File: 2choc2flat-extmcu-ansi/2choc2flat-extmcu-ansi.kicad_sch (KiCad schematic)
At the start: 138 parts, among them J1 Conn_01x09_Male, J2 Conn_01x05_Male, J3 Conn_01x09_Male, K1 KEYSW, K10 KEYSW, K11 KEYSW, K12 KEYSW, K13 KEYSW, K14 KEYSW, K16 KEYSW, K17 KEYSW, K18 KEYSW, K19 KEYSW, K2 KEYSW, K20 KEYSW, K21 KEYSW, K22 KEYSW, K23 KEYSW, K24 KEYSW, K25 KEYSW, K26 KEYSW, K27 KEYSW, K28 KEYSW, K29 KEYSW, K3 KEYSW, K31 KEYSW, K31-1 KEYSW, K32 KEYSW, K33 KEYSW, K34 KEYSW, K35 KEYSW, K36 KEYSW, K37 KEYSW, K38 KEYSW, K39 KEYSW, K4 KEYSW, K40 KEYSW, K41 KEYSW, K42 KEYSW, K44 KEYSW, K46 KEYSW, K47 KEYSW, K48 KEYSW, K49 KEYSW, K5 KEYSW, K50 KEYSW, K51 KEYSW, K52 KEYSW, K53 KEYSW, K54 KEYSW, K55 KEYSW, K56 KEYSW, K57 KEYSW, K58 KEYSW, K59 KEYSW, K6 KEYSW, K61 KEYSW, K62 KEYSW, K63 KEYSW, K67 KEYSW, K7 KEYSW, K71 KEYSW, K72 KEYSW, K73 KEYSW, K74 KEYSW, K75 KEYSW, K8 KEYSW, K9 KEYSW

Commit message: fix stab orientation to plate
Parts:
- K67: footprint Switch_Keyboard_Hotswap_Kailh_mine:SW_Hotswap_Kailh_Choc_V2_6.25u_North_Gateron_LP_Stabs -> Switch_Keyboard_Hotswap_Kailh_mine:SW_Hotswap_Kailh_Choc_V2_6.25u
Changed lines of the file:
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@@
       (effects (font (size 1.524 1.524)) hide)
     )
-    (property "Footprint" "Switch_Keyboard_Hotswap_Kailh_mine:SW_Hotswap_Kailh_Choc_V2_6.25u_North_Gateron_LP_Stabs" (id 2) (at 161.29 222.25 0)
+    (property "Footprint" "Switch_Keyboard_Hotswap_Kailh_mine:SW_Hotswap_Kailh_Choc_V2_6.25u" (id 2) (at 161.29 222.25 0)
       (effects (font (size 1.524 1.524)) hide)
     )
@@
     )
     (path "/00000000-0000-0000-0000-00005c555e38"
-      (reference "K67") (unit 1) (value "KEYSW") (footprint "Switch_Keyboard_Hotswap_Kailh_mine:SW_Hotswap_Kailh_Choc_V2_6.25u_North_Gateron_LP_Stabs")
+      (reference "K67") (unit 1) (value "KEYSW") (footprint "Switch_Keyboard_Hotswap_Kailh_mine:SW_Hotswap_Kailh_Choc_V2_6.25u")
     )
     (path "/00000000-0000-0000-0000-00005cb7e685"

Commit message: wip attempting rerouting
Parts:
- added DI1: LED, LED_SMD:LED_1206_3216Metric_ReverseMount_Hole1.8x2.4mm, symbol Device:LED
- added R1: 330R, Resistor_SMD:R_0603_1608Metric, symbol Device:R_Small_US
- D1, D10, D11, D12, D13, D14, D16, D17, D18, D19, D2, D20, D21, D22, D23, D24, D25, D26, D27, D28, D29, D3, D31, D32, D33, D34, D35, D36, D37, D38, D39, D4, D40, D41, D42, D44, D46, D47, D48, D49, D5, D50, D51, D52, D53, D54, D55, D56, D57, D58, D59, D6, D61, D62, D63, D67, D7, D71, D72, D73, D74, D75, D8, D9: footprint Diode_SMD:D_0805_2012Metric -> Diode_SMD:D_SOD-323_HandSoldering
- K8: footprint Switch_Keyboard_Kailh_mine:SW_Kailh_Choc_V2_1.00u -> Switch_Keyboard_Hotswap_Kailh_mine:SW_Hotswap_Kailh_Choc_V2_1.00u
- S3: footprint MountingHole:MountingHole_2.2mm_M2_Pad_TopOnly -> MountingHole:MountingHole_2.2mm_M2_Pad_Via
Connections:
- net +3V3: now also J3.3 (Pin_3); no longer J1.3 (Pin_3)
- net +5V: now also J3.1 (Pin_1); no longer J1.1 (Pin_1)
- net GND: now also J3.2 (Pin_2), DI1.1 (K); no longer J1.2 (Pin_2)
- net col0: now also J3.9 (Pin_9), K16.1, K46.1, K61.1; no longer J1.4 (Pin_4), K16.2, K46.2, K61.2
- net col1: now also J3.4 (Pin_4), K17.1, K2.1, K32.1, K47.1; no longer J1.5 (Pin_5), K17.2, K2.2, K32.2, K47.2
- net col10: now also J1.5 (Pin_5); no longer J3.5 (Pin_5)
- net col11: now also J1.4 (Pin_4); no longer J3.4 (Pin_4)
- net col12: now also J1.3 (Pin_3); no longer J3.3 (Pin_3)
- net col13: now also J1.2 (Pin_2), K29.1, K44.1; no longer J3.2 (Pin_2), K29.2, K44.2
- net col2: now also J3.5 (Pin_5), K3.1, K48.1, K63.1; no longer J1.6 (Pin_6), K3.2, K48.2, K63.2
- net col3: now also J3.6 (Pin_6); no longer J1.7 (Pin_7)
- net col4: now also J3.7 (Pin_7); no longer J1.8 (Pin_8)
- net col5: now also J3.8 (Pin_8); no longer J1.9 (Pin_9)
- net col6: now also K37.1, K67.1; no longer K37.2, K67.2
- net col8: now also J1.7 (Pin_7); no longer J3.7 (Pin_7)
- net col9: now also J1.6 (Pin_6), K71.1; no longer J3.6 (Pin_6), K71.2
- net row3: now also J1.9 (Pin_9); no longer J3.9 (Pin_9)
- net row4: now also J1.8 (Pin_8); no longer J3.8 (Pin_8)
- net at D2.2 (A): now also K2.2; no longer K2.1
- net at D3.2 (A): now also K3.2; no longer K3.1
- net at D16.2 (A): now also K16.2; no longer K16.1
- net at D17.2 (A): now also K17.2; no longer K17.1
- net at D29.2 (A): now also K29.2; no longer K29.1
- net at D32.2 (A): now also K32.2; no longer K32.1
- net at D37.2 (A): now also K37.2; no longer K37.1
- net at D44.2 (A): now also K44.2; no longer K44.1
- net at D46.2 (A): now also K46.2; no longer K46.1
- net at D48.2 (A): now also K48.2; no longer K48.1
- net at D61.2 (A): now also K61.2; no longer K61.1
- net at D63.2 (A): now also K63.2; no longer K63.1
- net at D67.2 (A): now also K67.2; no longer K67.1
- net at D71.2 (A): now also K71.2; no longer K71.1
- net at D47.2 (A): now also K47.2; no longer K47.1
- new net: DI1.2 (A), R1.2
- new net caps: J1.1 (Pin_1), R1.1
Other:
- moved on the sheet: K44

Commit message: routing complete
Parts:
- S3: footprint MountingHole:MountingHole_2.2mm_M2_Pad_Via -> MountingHole:MountingHole_2.2mm_M2_Pad_TopOnly
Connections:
- net col0: now also J3.4 (Pin_4); no longer J3.9 (Pin_9)
- net col1: now also J3.5 (Pin_5); no longer J3.4 (Pin_4)
- net col10: now also J1.4 (Pin_4); no longer J1.5 (Pin_5)
- net col11: now also J1.5 (Pin_5); no longer J1.4 (Pin_4)
- net col12: now also J1.6 (Pin_6); no longer J1.3 (Pin_3)
- net col13: now also J1.7 (Pin_7); no longer J1.2 (Pin_2)
- net col2: now also J3.6 (Pin_6); no longer J3.5 (Pin_5)
- net col3: now also J3.7 (Pin_7); no longer J3.6 (Pin_6)
- net col4: now also J3.8 (Pin_8); no longer J3.7 (Pin_7)
- net col5: now also J3.9 (Pin_9); no longer J3.8 (Pin_8)
- net col6: now also J2.5 (Pin_5); no longer J2.4 (Pin_4)
- net col7: now also J2.4 (Pin_4); no longer J2.5 (Pin_5)
- net col8: now also J1.2 (Pin_2); no longer J1.7 (Pin_7)
- net col9: now also J1.3 (Pin_3); no longer J1.6 (Pin_6)
- net row0: now also J2.3 (Pin_3); no longer J2.1 (Pin_1)
- net row2: now also J2.1 (Pin_1); no longer J2.3 (Pin_3)

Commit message: rev 1.3 layouts
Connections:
- net col10: now also J1.5 (Pin_5); no longer J1.4 (Pin_4)
- net col11: now also J1.4 (Pin_4); no longer J1.5 (Pin_5)
- net col12: now also J1.3 (Pin_3); no longer J1.6 (Pin_6)
- net col13: now also J1.2 (Pin_2); no longer J1.7 (Pin_7)
- net col8: now also J1.7 (Pin_7); no longer J1.2 (Pin_2)
- net col9: now also J1.6 (Pin_6); no longer J1.3 (Pin_3)

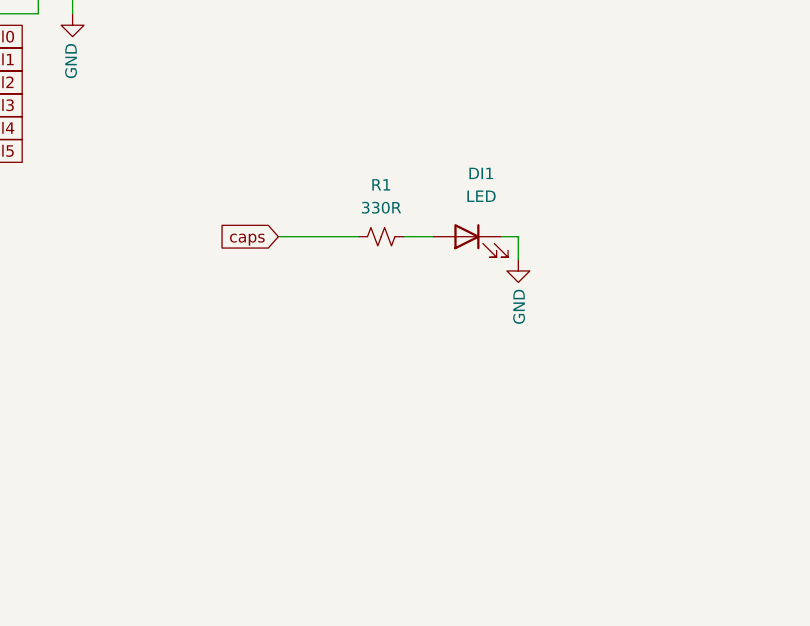
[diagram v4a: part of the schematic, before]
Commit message: add second caps led, minor tweaks
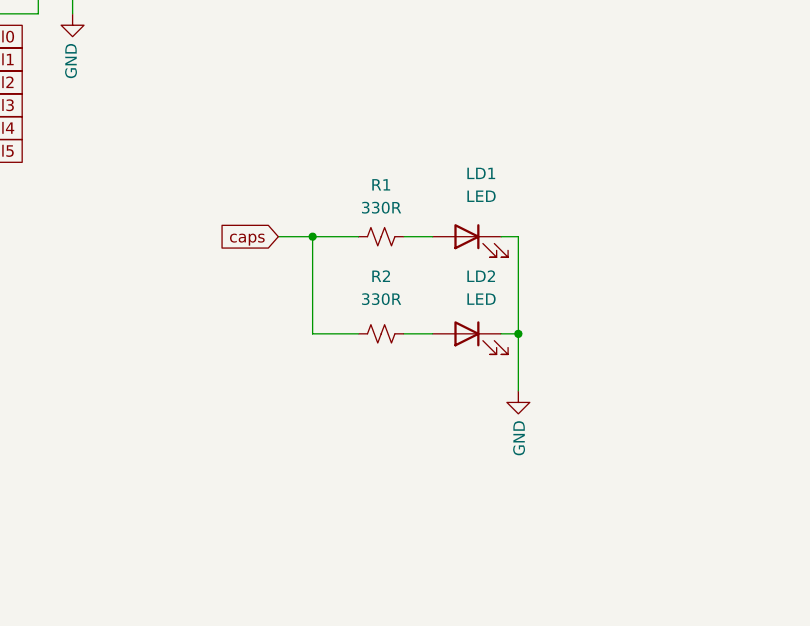
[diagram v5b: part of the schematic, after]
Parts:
- added LD2: LED, LED_SMD:LED_1206_3216Metric_ReverseMount_Hole1.8x2.4mm, symbol Device:LED
- added R2: 330R, Resistor_SMD:R_0603_1608Metric, symbol Device:R_Small_US
- renumbered DI1 to LD1
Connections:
- net GND: now also LD2.1 (K)
- net caps: now also R2.1
- new net: LD2.2 (A), R2.2
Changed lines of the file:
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@@
   (junction (at 311.15 161.29) (diameter 0) (color 0 0 0 0)
   )
+  (junction (at 163.83 87.63) (diameter 0) (color 0 0 0 0)
+  )
   (junction (at 87.63 146.05) (diameter 0) (color 0 0 0 0)
   )
@@
   (junction (at 270.51 146.05) (diameter 0) (color 0 0 0 0)
   )
+  (junction (at 140.97 76.835) (diameter 0) (color 0 0 0 0)
+  )
   (junction (at 250.19 201.93) (diameter 0) (color 0 0 0 0)
   )
@@
     (stroke (width 0) (type default) (color 0 0 0 0))
   )
+  (wire (pts (xy 140.97 87.63) (xy 146.05 87.63))
+    (stroke (width 0) (type default) (color 0 0 0 0))
+  )
   (wire (pts (xy 29.21 222.25) (xy 31.75 222.25))
     (stroke (width 0) (type default) (color 0 0 0 0))
@@
     (stroke (width 0) (type default) (color 0 0 0 0))
   )
+  (wire (pts (xy 163.83 87.63) (xy 163.83 93.98))
+    (stroke (width 0) (type default) (color 0 0 0 0))
+  )
   (wire (pts (xy 252.73 161.29) (xy 255.27 161.29))
     (stroke (width 0) (type default) (color 0 0 0 0))
@@
     (stroke (width 0) (type default) (color 0 0 0 0))
   )
-  (wire (pts (xy 163.83 76.835) (xy 163.83 79.375))
+  (wire (pts (xy 163.83 76.835) (xy 163.83 87.63))
     (stroke (width 0) (type default) (color 0 0 0 0))
   )
@@
     (stroke (width 0) (type default) (color 0 0 0 0))
   )
+  (wire (pts (xy 140.97 76.835) (xy 146.05 76.835))
+    (stroke (width 0) (type default) (color 0 0 0 0))
+  )
   (wire (pts (xy 110.49 52.07) (xy 101.6 52.07))
     (stroke (width 0) (type default) (color 0 0 0 0))
@@
     (stroke (width 0) (type default) (color 0 0 0 0))
   )
+  (wire (pts (xy 151.13 87.63) (xy 154.305 87.63))
+    (stroke (width 0) (type default) (color 0 0 0 0))
+  )
   (wire (pts (xy 171.45 184.15) (xy 171.45 181.61))
     (stroke (width 0) (type default) (color 0 0 0 0))
@@
     (stroke (width 0) (type default) (color 0 0 0 0))
   )
-  (wire (pts (xy 137.16 76.835) (xy 146.05 76.835))
+  (wire (pts (xy 137.16 76.835) (xy 140.97 76.835))
     (stroke (width 0) (type default) (color 0 0 0 0))
   )
@@
     (stroke (width 0) (type default) (color 0 0 0 0))
   )
+  (wire (pts (xy 161.925 87.63) (xy 163.83 87.63))
+    (stroke (width 0) (type default) (color 0 0 0 0))
+  )
   (wire (pts (xy 171.45 204.47) (xy 171.45 201.93))
     (stroke (width 0) (type default) (color 0 0 0 0))
@@
     (stroke (width 0) (type default) (color 0 0 0 0))
   )
+  (wire (pts (xy 140.97 76.835) (xy 140.97 87.63))
+    (stroke (width 0) (type default) (color 0 0 0 0))
+  )
   (global_label "col8" (shape input) (at 209.55 130.81 180)
     (effects (font (size 1.27 1.27)) (justify right))
@@
     (pin "2")
   )
-  (symbol (lib_id "Power:GND") (at 163.83 79.375 0) (unit 1)
+  (symbol (lib_id "Power:GND") (at 163.83 93.98 0) (unit 1)
     (in_bom yes) (on_board yes)
-    (property "Reference" "#PWR0103" (id 0) (at 163.83 85.725 0)
+    (property "Reference" "#PWR0103" (id 0) (at 163.83 100.33 0)
       (effects (font (size 1.27 1.27)) hide)
     )
-    (property "Value" "GND" (id 1) (at 163.957 82.6262 90)
+    (property "Value" "GND" (id 1) (at 163.957 97.2312 90)
       (effects (font (size 1.27 1.27)) (justify right))
     )
-    (property "Footprint" "" (id 2) (at 163.83 79.375 0)
+    (property "Footprint" "" (id 2) (at 163.83 93.98 0)
+      (effects (font (size 1.27 1.27)) hide)
+    )
+    (property "Datasheet" "" (id 3) (at 163.83 93.98 0)
+      (effects (font (size 1.27 1.27)) hide)
+    )
+    (pin "1")
+  )
+  (symbol (lib_id "Device:R_Small_US") (at 148.59 87.63 90) (unit 1)
+    (in_bom yes) (on_board yes) (fields_autoplaced)
+    (property "Reference" "R2" (id 0) (at 148.59 81.28 90))
+    (property "Value" "330R" (id 1) (at 148.59 83.82 90))
+    (property "Footprint" "Resistor_SMD:R_0603_1608Metric" (id 2) (at 148.59 87.63 0)
       (effects (font (size 1.27 1.27)) hide)
     )
-    (property "Datasheet" "" (id 3) (at 163.83 79.375 0)
+    (property "Datasheet" "~" (id 3) (at 148.59 87.63 0)
       (effects (font (size 1.27 1.27)) hide)
     )
     (pin "1")
+    (pin "2")
   )
   (symbol (lib_id "Connector:Conn_01x09_Male") (at 81.28 57.15 0) (mirror y) (unit 1)
@@
     (pin "1")
   )
+  (symbol (lib_id "Device:LED") (at 158.115 87.63 0) (mirror y) (unit 1)
+    (in_bom yes) (on_board yes) (fields_autoplaced)
+    (property "Reference" "LD2" (id 0) (at 159.7025 81.28 0))
+    (property "Value" "LED" (id 1) (at 159.7025 83.82 0))
+    (property "Footprint" "LED_SMD:LED_1206_3216Metric_ReverseMount_Hole1.8x2.4mm" (id 2) (at 158.115 87.63 0)
+      (effects (font (size 1.27 1.27)) hide)
+    )
+    (property "Datasheet" "~" (id 3) (at 158.115 87.63 0)
+      (effects (font (size 1.27 1.27)) hide)
+    )
+    (pin "1")
+    (pin "2")
+  )
   (symbol (lib_id "Connector:Conn_01x09_Male") (at 96.52 57.15 0) (unit 1)
     (in_bom yes) (on_board yes)
@@
   (symbol (lib_id "Device:LED") (at 158.115 76.835 0) (mirror y) (unit 1)
     (in_bom yes) (on_board yes) (fields_autoplaced)
-    (property "Reference" "DI1" (id 0) (at 159.7025 69.85 0))
+    (property "Reference" "LD1" (id 0) (at 159.7025 69.85 0))
     (property "Value" "LED" (id 1) (at 159.7025 72.39 0))
     (property "Footprint" "LED_SMD:LED_1206_3216Metric_ReverseMount_Hole1.8x2.4mm" (id 2) (at 158.115 76.835 0)
@@
       (reference "D75") (unit 1) (value "D") (footprint "Diode_SMD:D_SOD-323_HandSoldering")
     )
-    (path "/d2a931d0-1ec6-4bb9-bddb-4815c7c34ed3"
-      (reference "DI1") (unit 1) (value "LED") (footprint "LED_SMD:LED_1206_3216Metric_ReverseMount_Hole1.8x2.4mm")
-    )
     (path "/339b77fe-16f3-43b4-8399-7230a8ae2102"
       (reference "J1") (unit 1) (value "Conn_01x09_Male") (footprint "Connector_PinHeader_2.54mm:PinHeader_1x09_P2.54mm_Vertical")
@@
       (reference "K75") (unit 1) (value "KEYSW") (footprint "Switch_Keyboard_Hotswap_Kailh_mine:SW_Hotswap_Kailh_Choc_V2_1.00u")
     )
+    (path "/d2a931d0-1ec6-4bb9-bddb-4815c7c34ed3"
+      (reference "LD1") (unit 1) (value "LED") (footprint "LED_SMD:LED_1206_3216Metric_ReverseMount_Hole1.8x2.4mm")
+    )
+    (path "/b7f1724b-1d47-4bd9-8c41-10c52964ecee"
+      (reference "LD2") (unit 1) (value "LED") (footprint "LED_SMD:LED_1206_3216Metric_ReverseMount_Hole1.8x2.4mm")
+    )
     (path "/8d5f9bef-ee8d-4e8f-a9d6-9a7508b7e457"
       (reference "R1") (unit 1) (value "330R") (footprint "Resistor_SMD:R_0603_1608Metric")
     )
+    (path "/31bcc252-1418-4877-b5ef-6cba8a364cba"
+      (reference "R2") (unit 1) (value "330R") (footprint "Resistor_SMD:R_0603_1608Metric")
+    )
     (path "/00000000-0000-0000-0000-00005c2a7b35"

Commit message: wip v1.4 ansi
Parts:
- LD1, LD2: footprint LED_SMD:LED_1206_3216Metric_ReverseMount_Hole1.8x2.4mm -> schizobovine:LED_1206_3216Metric_ReverseMount_Hole1.8x2.4mm
- S1, S2, S6: footprint footprints:5.5_5x2.5mm -> schizobovine:3_5x2.5mm
- S3: footprint MountingHole:MountingHole_2.2mm_M2_Pad_TopOnly -> schizobovine:MountingHole_2.2mm_M2_Pad_TopOnly
- S4, S5: footprint footprints:10x5_7x2.5mm -> schizobovine:8x3.5_7x2.5mm
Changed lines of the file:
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@@
       (effects (font (size 1.27 1.27)) (justify left))
     )
-    (property "Footprint" "footprints:5.5_5x2.5mm" (id 2) (at 234.95 25.4 0)
+    (property "Footprint" "schizobovine:3_5x2.5mm" (id 2) (at 234.95 25.4 0)
       (effects (font (size 1.27 1.27)) hide)
     )
@@
       (effects (font (size 1.27 1.27)) (justify left))
     )
-    (property "Footprint" "footprints:5.5_5x2.5mm" (id 2) (at 234.95 31.75 0)
+    (property "Footprint" "schizobovine:3_5x2.5mm" (id 2) (at 234.95 31.75 0)
       (effects (font (size 1.27 1.27)) hide)
     )
@@
       (effects (font (size 1.27 1.27)) (justify left))
     )
-    (property "Footprint" "MountingHole:MountingHole_2.2mm_M2_Pad_TopOnly" (id 2) (at 234.95 38.1 0)
+    (property "Footprint" "schizobovine:MountingHole_2.2mm_M2_Pad_TopOnly" (id 2) (at 234.95 38.1 0)
       (effects (font (size 1.27 1.27)) hide)
     )
@@
       (effects (font (size 1.27 1.27)) (justify left))
     )
-    (property "Footprint" "footprints:10x5_7x2.5mm" (id 2) (at 234.95 44.45 0)
+    (property "Footprint" "schizobovine:8x3.5_7x2.5mm" (id 2) (at 234.95 44.45 0)
       (effects (font (size 1.27 1.27)) hide)
     )
@@
       (effects (font (size 1.27 1.27)) (justify left))
     )
-    (property "Footprint" "footprints:10x5_7x2.5mm" (id 2) (at 234.95 50.8 0)
+    (property "Footprint" "schizobovine:8x3.5_7x2.5mm" (id 2) (at 234.95 50.8 0)
       (effects (font (size 1.27 1.27)) hide)
     )
@@
       (effects (font (size 1.27 1.27)) (justify left))
     )
-    (property "Footprint" "footprints:5.5_5x2.5mm" (id 2) (at 234.95 57.15 0)
+    (property "Footprint" "schizobovine:3_5x2.5mm" (id 2) (at 234.95 57.15 0)
       (effects (font (size 1.27 1.27)) hide)
     )
@@
     (property "Reference" "LD2" (id 0) (at 159.7025 81.28 0))
     (property "Value" "LED" (id 1) (at 159.7025 83.82 0))
-    (property "Footprint" "LED_SMD:LED_1206_3216Metric_ReverseMount_Hole1.8x2.4mm" (id 2) (at 158.115 87.63 0)
+    (property "Footprint" "schizobovine:LED_1206_3216Metric_ReverseMount_Hole1.8x2.4mm" (id 2) (at 158.115 87.63 0)
       (effects (font (size 1.27 1.27)) hide)
     )
@@
     (property "Reference" "LD1" (id 0) (at 159.7025 69.85 0))
     (property "Value" "LED" (id 1) (at 159.7025 72.39 0))
-    (property "Footprint" "LED_SMD:LED_1206_3216Metric_ReverseMount_Hole1.8x2.4mm" (id 2) (at 158.115 76.835 0)
+    (property "Footprint" "schizobovine:LED_1206_3216Metric_ReverseMount_Hole1.8x2.4mm" (id 2) (at 158.115 76.835 0)
       (effects (font (size 1.27 1.27)) hide)
     )
@@
     )
     (path "/d2a931d0-1ec6-4bb9-bddb-4815c7c34ed3"
-      (reference "LD1") (unit 1) (value "LED") (footprint "LED_SMD:LED_1206_3216Metric_ReverseMount_Hole1.8x2.4mm")
+      (reference "LD1") (unit 1) (value "LED") (footprint "schizobovine:LED_1206_3216Metric_ReverseMount_Hole1.8x2.4mm")
     )
     (path "/b7f1724b-1d47-4bd9-8c41-10c52964ecee"
-      (reference "LD2") (unit 1) (value "LED") (footprint "LED_SMD:LED_1206_3216Metric_ReverseMount_Hole1.8x2.4mm")
+      (reference "LD2") (unit 1) (value "LED") (footprint "schizobovine:LED_1206_3216Metric_ReverseMount_Hole1.8x2.4mm")
     )
     (path "/8d5f9bef-ee8d-4e8f-a9d6-9a7508b7e457"
@@
     )
     (path "/00000000-0000-0000-0000-00005c2a7b35"
-      (reference "S1") (unit 1) (value "Screw") (footprint "footprints:5.5_5x2.5mm")
+      (reference "S1") (unit 1) (value "Screw") (footprint "schizobovine:3_5x2.5mm")
     )
     (path "/00000000-0000-0000-0000-00005c2aa553"
-      (reference "S2") (unit 1) (value "Screw") (footprint "footprints:5.5_5x2.5mm")
+      (reference "S2") (unit 1) (value "Screw") (footprint "schizobovine:3_5x2.5mm")
     )
     (path "/00000000-0000-0000-0000-00005c2cd859"
-      (reference "S3") (unit 1) (value "Screw") (footprint "MountingHole:MountingHole_2.2mm_M2_Pad_TopOnly")
+      (reference "S3") (unit 1) (value "Screw") (footprint "schizobovine:MountingHole_2.2mm_M2_Pad_TopOnly")
     )
     (path "/00000000-0000-0000-0000-00005c2f0889"
-      (reference "S4") (unit 1) (value "Screw") (footprint "footprints:10x5_7x2.5mm")
+      (reference "S4") (unit 1) (value "Screw") (footprint "schizobovine:8x3.5_7x2.5mm")
     )
     (path "/00000000-0000-0000-0000-00005c313929"
-      (reference "S5") (unit 1) (value "Screw") (footprint "footprints:10x5_7x2.5mm")
+      (reference "S5") (unit 1) (value "Screw") (footprint "schizobovine:8x3.5_7x2.5mm")
     )
     (path "/00000000-0000-0000-0000-00005c3372c8"
-      (reference "S6") (unit 1) (value "Screw") (footprint "footprints:5.5_5x2.5mm")
-    )
-  )
+      (reference "S6") (unit 1) (value "Screw") (footprint "schizobovine:3_5x2.5mm")
+    )
+  )
